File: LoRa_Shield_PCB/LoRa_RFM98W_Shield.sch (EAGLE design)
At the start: 40 parts, among them IC2 TXS0102DCUR, IC3 SHT20, J1 TYPE-C-31-M-17, J2 CON_TERMINAL_BLOCK_03-5MM, U1 XC6206P332MR, U2 RFM98W, X1 BU-SMA-H

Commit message: PCB production V1.0.0
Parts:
- renumbered IC3 to IC1
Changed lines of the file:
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@@
 <part name="LED1" library="led" library_urn="urn:adsk.eagle:library:259" deviceset="LED" device="CHIPLED_0805" package3d_urn="urn:adsk.eagle:package:15821/2"/>
 <part name="U1" library="SamacSys_Parts" deviceset="XC6206P332MR" device=""/>
-<part name="IC3" library="SamacSys_Parts" deviceset="SHT20" device=""/>
+<part name="IC1" library="SamacSys_Parts" deviceset="SHT20" device=""/>
 <part name="GND10" library="SparkFun-PowerSymbols" deviceset="GND" device=""/>
 </parts>
@@
 <attribute name="VALUE" x="242.824" y="63.5" size="1.778" layer="96" rot="R90" align="top-center"/>
 </instance>
-<instance part="IC3" gate="G$1" x="223.52" y="148.59" smashed="yes">
+<instance part="IC1" gate="G$1" x="223.52" y="148.59" smashed="yes">
 <attribute name="NAME" x="213.36" y="158.75" size="1.778" layer="95" align="center-left"/>
 <attribute name="VALUE" x="213.36" y="156.21" size="1.778" layer="96" align="center-left"/>
@@
 <wire x1="242.57" y1="163.83" x2="242.57" y2="158.75" width="0.1524" layer="91"/>
 <junction x="242.57" y="158.75"/>
-<pinref part="IC3" gate="G$1" pin="VSS"/>
+<pinref part="IC1" gate="G$1" pin="VSS"/>
 <wire x1="242.57" y1="152.4" x2="238.76" y2="152.4" width="0.1524" layer="91"/>
 </segment>
@@
 <pinref part="GND10" gate="1" pin="GND"/>
 <wire x1="223.52" y1="129.54" x2="223.52" y2="134.62" width="0.1524" layer="91"/>
-<pinref part="IC3" gate="G$1" pin="EP"/>
+<pinref part="IC1" gate="G$1" pin="EP"/>
 </segment>
 </net>
@@
 <wire x1="242.57" y1="142.24" x2="242.57" y2="146.05" width="0.1524" layer="91"/>
 <junction x="242.57" y="146.05"/>
-<pinref part="IC3" gate="G$1" pin="VDD"/>
+<pinref part="IC1" gate="G$1" pin="VDD"/>
 <wire x1="238.76" y1="149.86" x2="242.57" y2="149.86" width="0.1524" layer="91"/>
 </segment>
@@
 <wire x1="196.85" y1="153.67" x2="196.85" y2="152.4" width="0.1524" layer="91"/>
 <junction x="196.85" y="152.4"/>
-<pinref part="IC3" gate="G$1" pin="SDA"/>
+<pinref part="IC1" gate="G$1" pin="SDA"/>
 </segment>
 <segment>
@@
 <wire x1="201.93" y1="153.67" x2="201.93" y2="149.86" width="0.1524" layer="91"/>
 <junction x="201.93" y="149.86"/>
-<pinref part="IC3" gate="G$1" pin="SCL"/>
-</segment>
-<segment>
+<pinref part="IC1" gate="G$1" pin="SCL"/>
+</segment>
+<segment>

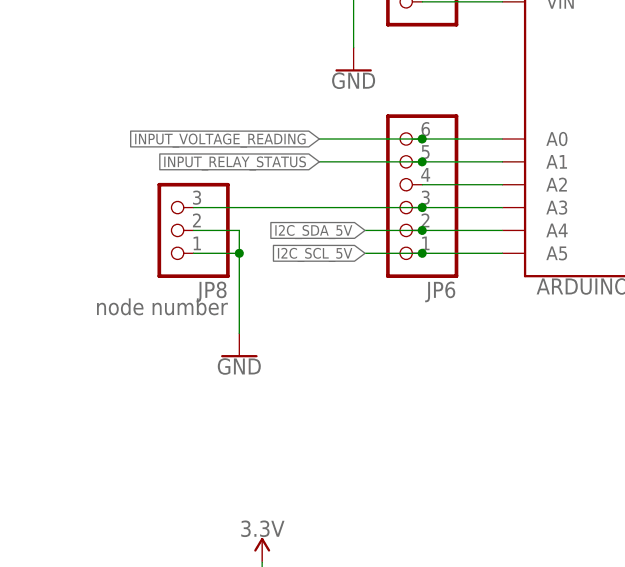
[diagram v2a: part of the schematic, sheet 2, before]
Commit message: schematic resistor value, arduino code
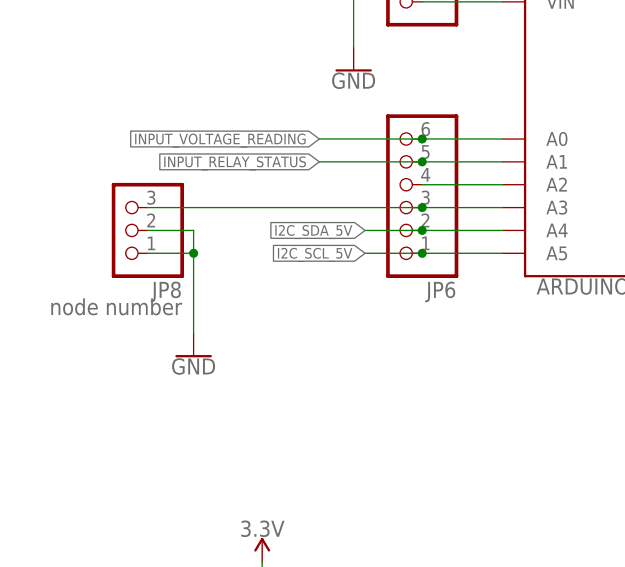
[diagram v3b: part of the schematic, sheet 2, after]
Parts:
- R2: value 165k -> 110k
- R4: value 15k -> 10k
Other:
- moved on the sheet: JP8
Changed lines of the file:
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@@
 <setting verticaltext="up"/>
 </settings>
-<grid distance="50" unitdist="mil" unit="mil" style="lines" multiple="1" display="no" altdistance="0.01" altunitdist="inch" altunit="inch"/>
+<grid distance="0.1" unitdist="inch" unit="inch" style="lines" multiple="1" display="no" altdistance="0.01" altunitdist="inch" altunit="inch"/>
 <layers>
 <layer number="1" name="Top" color="4" fill="1" visible="no" active="no"/>
@@
 <part name="J2" library="dp_devices" deviceset="CON_TERMINAL_BLOCK_03" device="-5MM"/>
 <part name="R3" library="rcl" library_urn="urn:adsk.eagle:library:334" deviceset="R-US_" device="R0603" package3d_urn="urn:adsk.eagle:package:23555/3" value="10k"/>
-<part name="R2" library="rcl" library_urn="urn:adsk.eagle:library:334" deviceset="R-US_" device="R0603" package3d_urn="urn:adsk.eagle:package:23555/3" value="165k"/>
-<part name="R4" library="rcl" library_urn="urn:adsk.eagle:library:334" deviceset="R-US_" device="R0603" package3d_urn="urn:adsk.eagle:package:23555/3" value="15k"/>
+<part name="R2" library="rcl" library_urn="urn:adsk.eagle:library:334" deviceset="R-US_" device="R0603" package3d_urn="urn:adsk.eagle:package:23555/3" value="110k"/>
+<part name="R4" library="rcl" library_urn="urn:adsk.eagle:library:334" deviceset="R-US_" device="R0603" package3d_urn="urn:adsk.eagle:package:23555/3" value="10k"/>
 <part name="GND16" library="SparkFun-PowerSymbols" deviceset="GND" device=""/>
 <part name="SUPPLY13" library="SparkFun-PowerSymbols" deviceset="5V" device=""/>
@@
 <attribute name="VALUE" x="68.58" y="20.066" size="1.778" layer="96" align="top-center"/>
 </instance>
-<instance part="GND9" gate="1" x="33.02" y="104.14" smashed="yes">
-<attribute name="VALUE" x="33.02" y="103.886" size="1.778" layer="96" align="top-center"/>
+<instance part="GND9" gate="1" x="27.94" y="104.14" smashed="yes">
+<attribute name="VALUE" x="27.94" y="103.886" size="1.778" layer="96" align="top-center"/>
 </instance>
 <instance part="GND1" gate="1" x="242.57" y="166.37" smashed="yes" rot="R180">
@@
 <attribute name="VALUE" x="248.92" y="95.504" size="1.778" layer="96" align="bottom-center"/>
 </instance>
-<instance part="JP8" gate="A" x="25.4" y="118.11" smashed="yes" rot="R180">
-<attribute name="NAME" x="31.75" y="112.395" size="1.778" layer="95" rot="R180"/>
-<attribute name="VALUE" x="31.75" y="110.49" size="1.778" layer="96" rot="R180"/>
+<instance part="JP8" gate="A" x="20.32" y="118.11" smashed="yes" rot="R180">
+<attribute name="NAME" x="26.67" y="112.395" size="1.778" layer="95" rot="R180"/>
+<attribute name="VALUE" x="26.67" y="110.49" size="1.778" layer="96" rot="R180"/>
 </instance>
 <instance part="R12" gate="G$1" x="231.14" y="41.91" smashed="yes">
@@
 <pinref part="GND9" gate="1" pin="GND"/>
 <pinref part="JP8" gate="A" pin="1"/>
-<wire x1="33.02" y1="106.68" x2="33.02" y2="115.57" width="0.1524" layer="91"/>
-<wire x1="33.02" y1="115.57" x2="27.94" y2="115.57" width="0.1524" layer="91"/>
+<wire x1="27.94" y1="106.68" x2="27.94" y2="115.57" width="0.1524" layer="91"/>
+<wire x1="27.94" y1="115.57" x2="22.86" y2="115.57" width="0.1524" layer="91"/>
 <pinref part="JP8" gate="A" pin="2"/>
-<wire x1="27.94" y1="118.11" x2="33.02" y2="118.11" width="0.1524" layer="91"/>
-<wire x1="33.02" y1="118.11" x2="33.02" y2="115.57" width="0.1524" layer="91"/>
-<junction x="33.02" y="115.57"/>
+<wire x1="22.86" y1="118.11" x2="27.94" y2="118.11" width="0.1524" layer="91"/>
+<wire x1="27.94" y1="118.11" x2="27.94" y2="115.57" width="0.1524" layer="91"/>
+<junction x="27.94" y="115.57"/>
 </segment>
 <segment>
@@
 <pinref part="JP6" gate="A" pin="3"/>
 <wire x1="62.23" y1="120.65" x2="53.34" y2="120.65" width="0.1524" layer="91"/>
-<wire x1="53.34" y1="120.65" x2="27.94" y2="120.65" width="0.1524" layer="91"/>
+<wire x1="53.34" y1="120.65" x2="22.86" y2="120.65" width="0.1524" layer="91"/>
 <junction x="53.34" y="120.65"/>
 <pinref part="JP8" gate="A" pin="3"/>
